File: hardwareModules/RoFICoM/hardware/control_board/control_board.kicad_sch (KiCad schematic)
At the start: 35 parts, among them J1 BoardSkirtConnector, J2 M+, J3 M-, J4 SYS_CONN, J5 PWR_CONN_1, J6 PWR_CONN_2, J7 CableConnector, J8 CablePads, J9 SkirtPads, U1 STM32G071GBU6, U2 DRV8837C, U3 HX6306P332MR, U4 KTH1611SH-SF5, U5 KTH1611SH-SF5

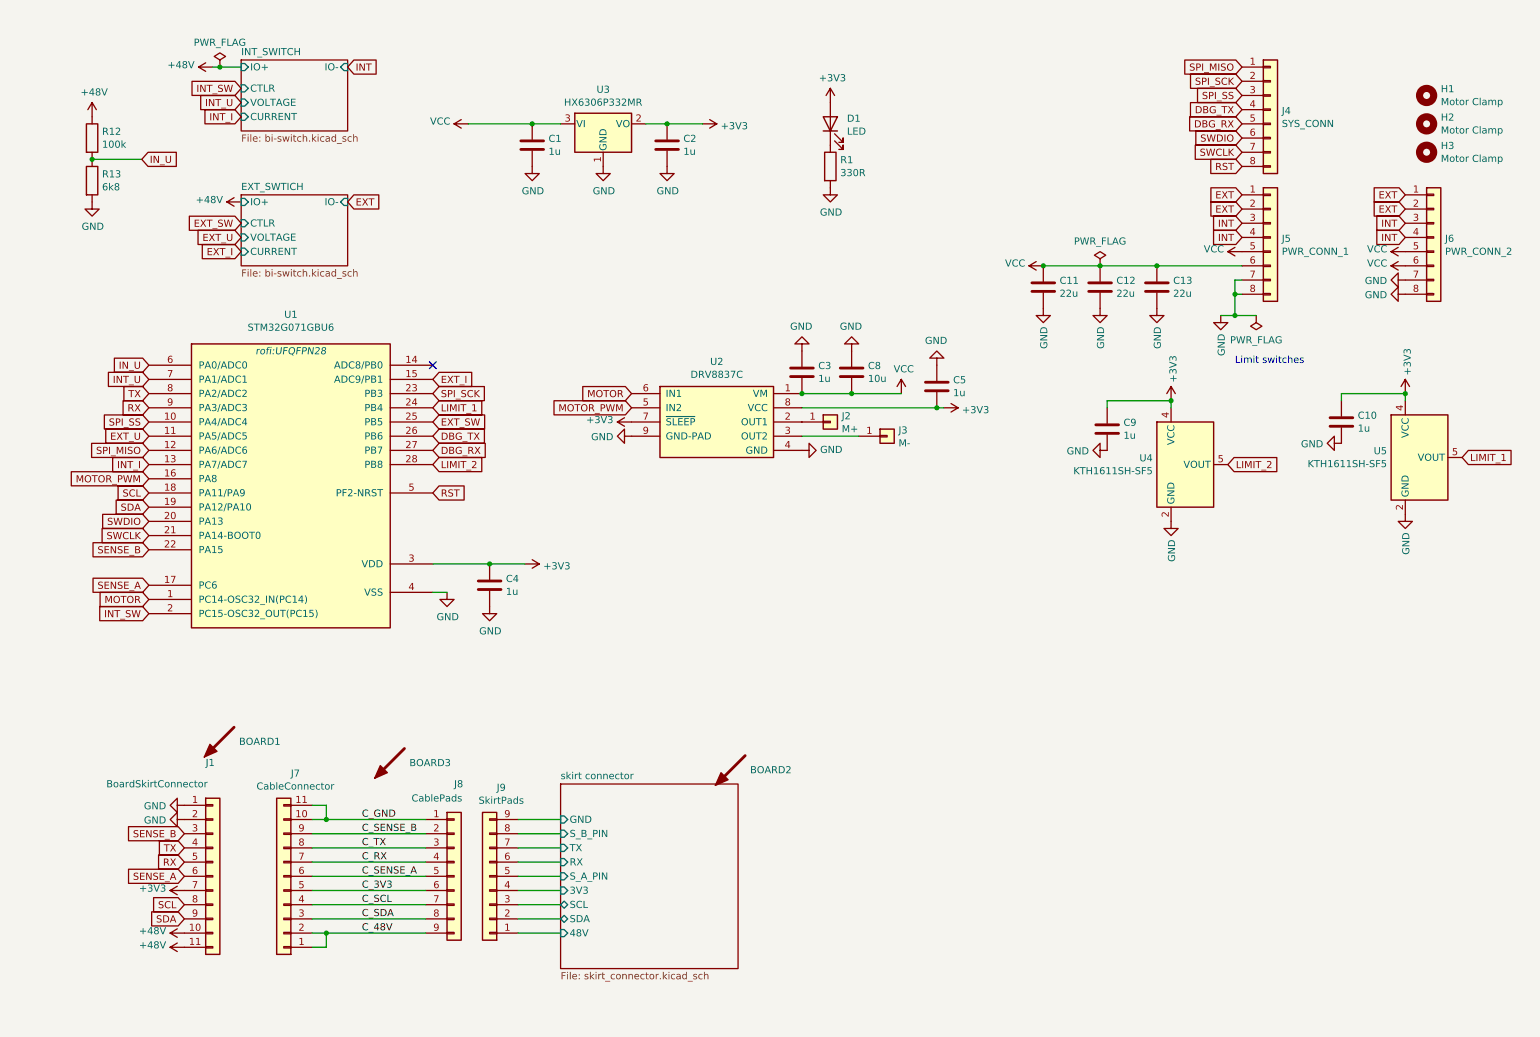
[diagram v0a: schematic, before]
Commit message: roficom: Implement v1 hardware
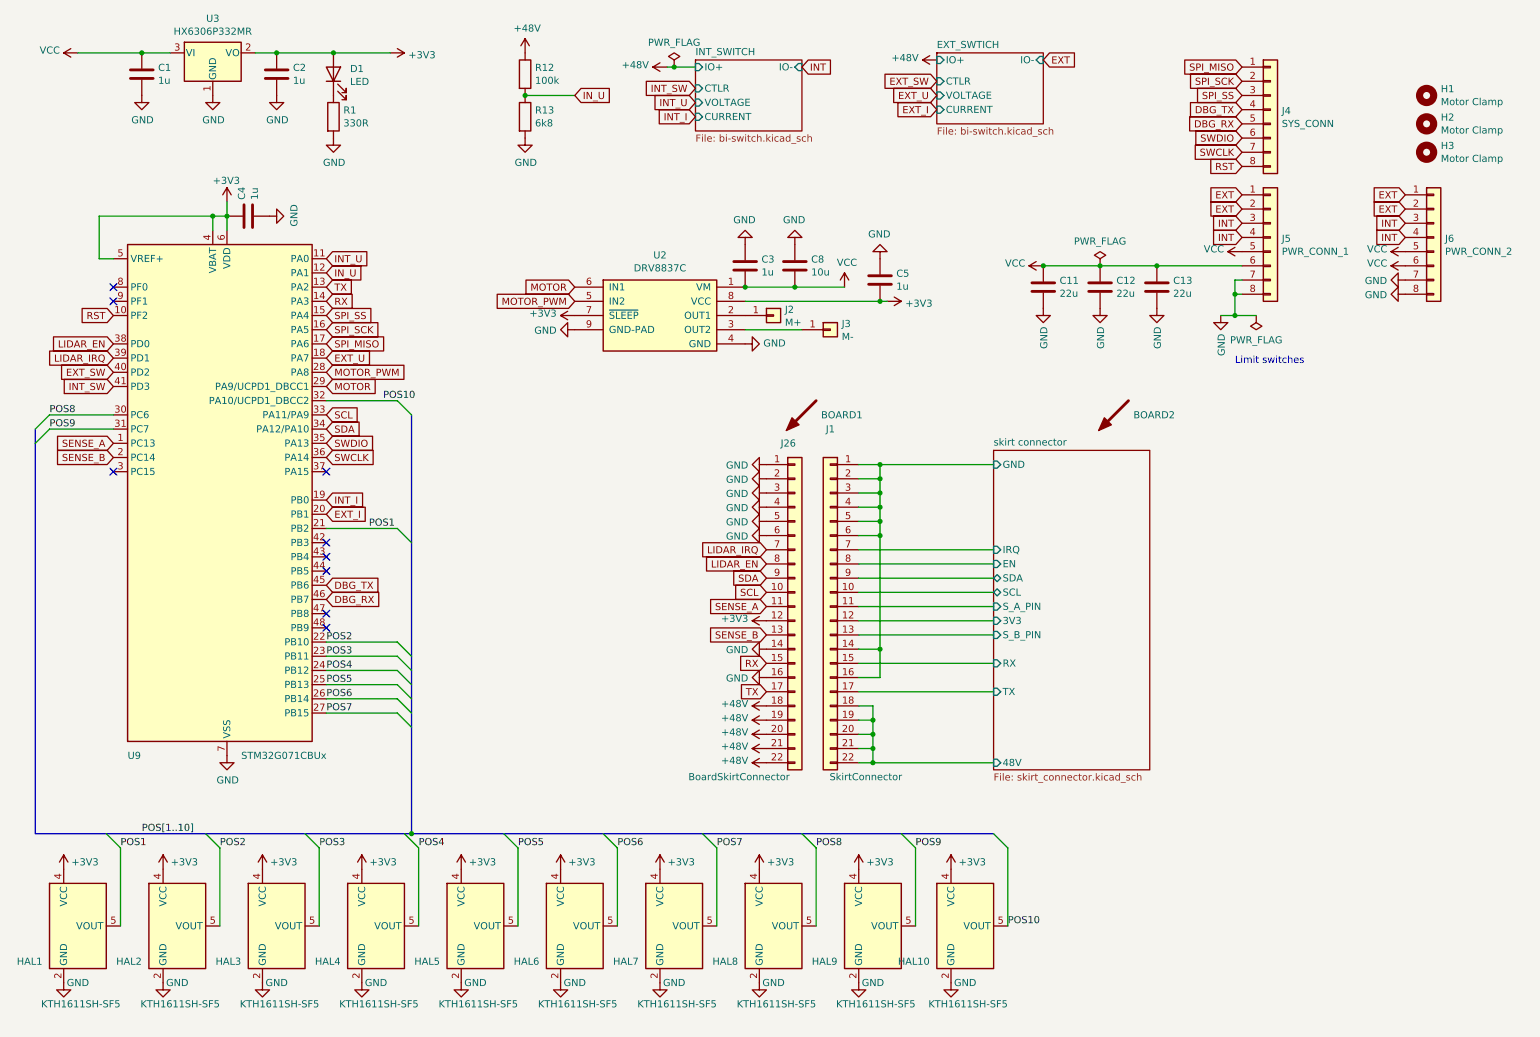
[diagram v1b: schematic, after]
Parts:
- removed BOARD3: BOARD, kikit:Board, symbol Graphic:SYM_Arrow45_Large
- removed C10, C9: 1u, Capacitor_SMD:C_0402_1005Metric, symbol Device:C
- removed J1: BoardSkirtConnector, rofi:FC38-11N1-AHK, symbol Connector_Generic:Conn_01x11
- removed J7: CableConnector, rofi:FPC_PADS_11, symbol Connector_Generic:Conn_01x11
- removed J8: CablePads, rofi:RoFICoM_CableFPCPads, symbol Connector_Generic:Conn_01x09
- removed J9: SkirtPads, rofi:RoFICoM_CablePads, symbol Connector_Generic:Conn_01x09
- removed U1: STM32G071GBU6, rofi:UFQFPN28, symbol rofi:STM32G071GBU6
- removed U4, U5: KTH1611SH-SF5, Package_TO_SOT_SMD:SOT-553, symbol rofi:KTH1611SH-SF5
- added HAL1, HAL10, HAL2, HAL3, HAL4, HAL5, HAL6, HAL7, HAL8, HAL9: KTH1611SH-SF5, Package_TO_SOT_SMD:SOT-553, symbol rofi:KTH1611SH-SF5
- added J1: SkirtConnector, rofi:FPC_0.5_22_PADS, symbol Connector_Generic:Conn_01x22
- added J26: BoardSkirtConnector, rofi:781272210, symbol Connector_Generic:Conn_01x22
- added U9: STM32G071CBUx, Package_DFN_QFN:QFN-48-1EP_7x7mm_P0.5mm_EP5.6x5.6mm, symbol STM32G0:STM32G071CBUx
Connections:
- net +3V3: now also HAL1.4 (VCC), HAL10.4 (VCC), HAL2.4 (VCC), HAL3.4 (VCC), HAL4.4 (VCC), HAL5.4 (VCC), HAL6.4 (VCC), HAL7.4 (VCC), HAL8.4 (VCC), HAL9.4 (VCC), J26.12 (Pin_12), U9.4 (VBAT), U9.5 (VREF+), U9.6 (VDD)
- net +48V: now also J26.18 (Pin_18), J26.19 (Pin_19), J26.20 (Pin_20), J26.21 (Pin_21), J26.22 (Pin_22)
- net DBG_RX: now also U9.46 (PB7)
- net DBG_TX: now also U9.45 (PB6)
- net EXT_I: now also U9.20 (PB1)
- net EXT_SW: now also U9.40 (PD2)
- net EXT_U: now also U9.18 (PA7)
- net GND: now also HAL1.2 (GND), HAL10.2 (GND), HAL2.2 (GND), HAL3.2 (GND), HAL4.2 (GND), HAL5.2 (GND), HAL6.2 (GND), HAL7.2 (GND), HAL8.2 (GND), HAL9.2 (GND), J26.1 (Pin_1), J26.14 (Pin_14), J26.16 (Pin_16), J26.2 (Pin_2), J26.3 (Pin_3), J26.4 (Pin_4), J26.5 (Pin_5), J26.6 (Pin_6), U9.49 (VSS), U9.7 (VSS)
- net INT_I: now also U9.19 (PB0)
- net INT_SW: now also U9.41 (PD3)
- net INT_U: now also U9.11 (PA0)
- net IN_U: now also U9.12 (PA1)
- net MOTOR: now also U9.29 (PA9/UCPD1_DBCC1)
- net MOTOR_PWM: now also U9.28 (PA8)
- net RST: now also U9.10 (PF2)
- net RX: now also J26.15 (Pin_15), U9.14 (PA3)
- net SCL: now also J26.10 (Pin_10), U9.33 (PA11/PA9)
- net SDA: now also J26.9 (Pin_9), U9.34 (PA12/PA10)
- net SENSE_A: now also J26.11 (Pin_11), U9.1 (PC13)
- net SENSE_B: now also J26.13 (Pin_13), U9.2 (PC14)
- net SPI_MISO: now also U9.17 (PA6)
- net SPI_SCK: now also U9.16 (PA5)
- net SPI_SS: now also U9.15 (PA4)
- net SWCLK: now also U9.36 (PA14)
- net SWDIO: now also U9.35 (PA13)
- net TX: now also J26.17 (Pin_17), U9.13 (PA2)
- net skirt connector/3V3: now also J1.12 (Pin_12)
- net skirt connector/48V: now also J1.18 (Pin_18), J1.19 (Pin_19), J1.20 (Pin_20), J1.21 (Pin_21), J1.22 (Pin_22)
- net skirt connector/GND: now also J1.1 (Pin_1), J1.14 (Pin_14), J1.16 (Pin_16), J1.2 (Pin_2), J1.3 (Pin_3), J1.4 (Pin_4), J1.5 (Pin_5), J1.6 (Pin_6)
- net skirt connector/RX: now also J1.15 (Pin_15)
- net skirt connector/SCL: now also J1.10 (Pin_10)
- net skirt connector/SDA: now also J1.9 (Pin_9)
- net skirt connector/S_A_PIN: now also J1.11 (Pin_11)
- net skirt connector/S_B_PIN: now also J1.13 (Pin_13)
- net skirt connector/TX: now also J1.17 (Pin_17)
- new net LIDAR_EN: J26.8 (Pin_8), U9.38 (PD0)
- new net LIDAR_IRQ: J26.7 (Pin_7), U9.39 (PD1)
- new net POS1: HAL1.5 (VOUT), U9.21 (PB2)
- new net POS10: HAL10.5 (VOUT), U9.32 (PA10/UCPD1_DBCC2)
- new net POS2: HAL2.5 (VOUT), U9.22 (PB10)
- new net POS3: HAL3.5 (VOUT), U9.23 (PB11)
- new net POS4: HAL4.5 (VOUT), U9.24 (PB12)
- new net POS5: HAL5.5 (VOUT), U9.25 (PB13)
- new net POS6: HAL6.5 (VOUT), U9.26 (PB14)
- new net POS7: HAL7.5 (VOUT), U9.27 (PB15)
- new net POS8: HAL8.5 (VOUT), U9.30 (PC6)
- new net POS9: HAL9.5 (VOUT), U9.31 (PC7)
- new net skirt connector/EN: J1.8 (Pin_8)
- new net skirt connector/IRQ: J1.7 (Pin_7)
- no-connect marks 1 -> 9
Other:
- sheet skirt connector ports: added EN, IRQ; removed none
- moved on the sheet: BOARD1, BOARD2, C1, C2, C3, C4, C5, C8, D1, J2, J3, R1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

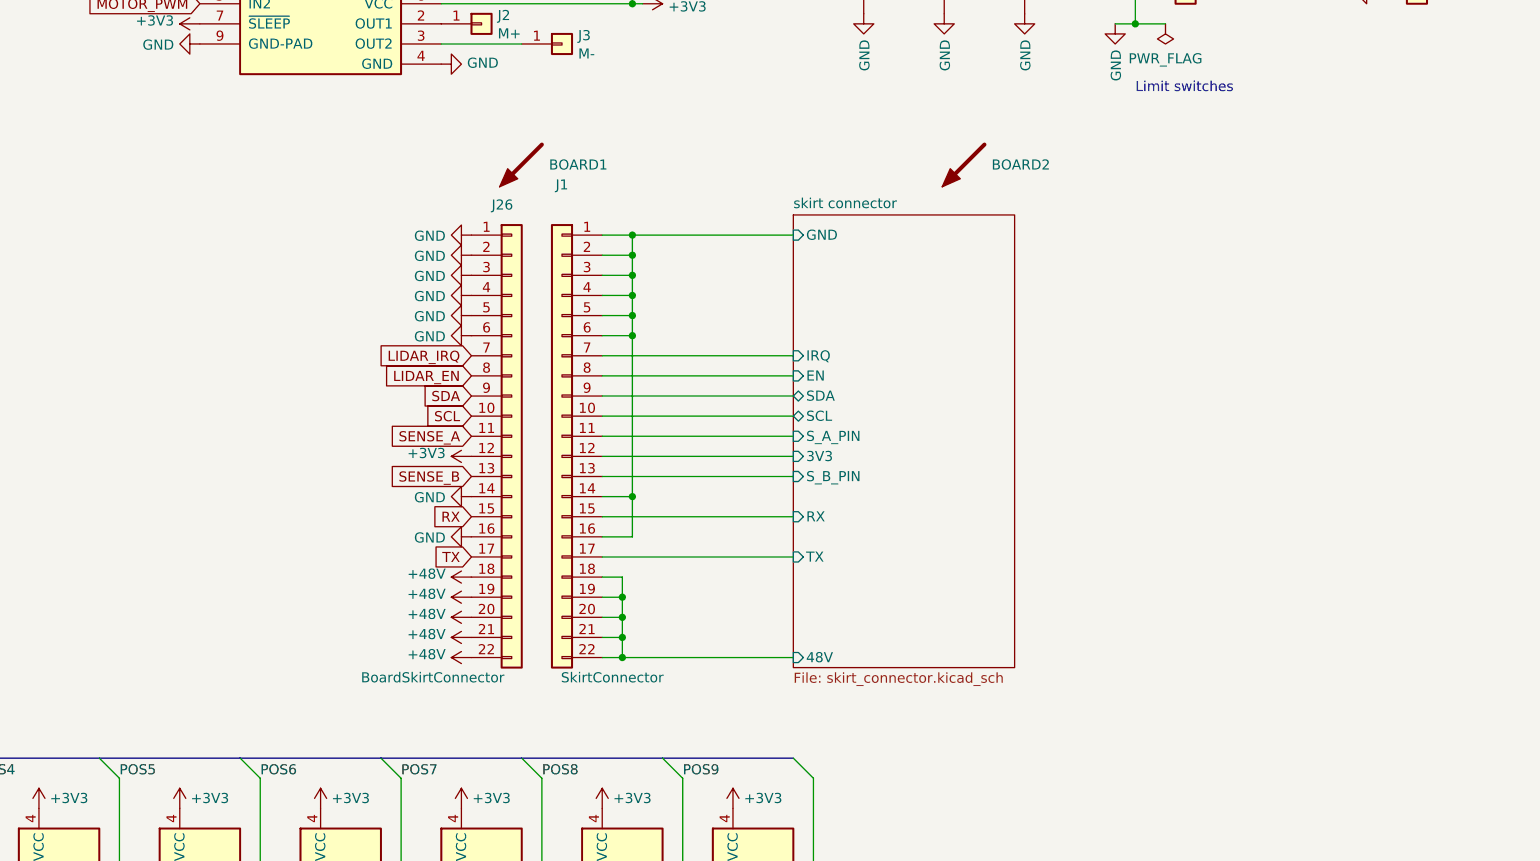
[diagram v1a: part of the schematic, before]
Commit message: hardware: Add custom FPC cables
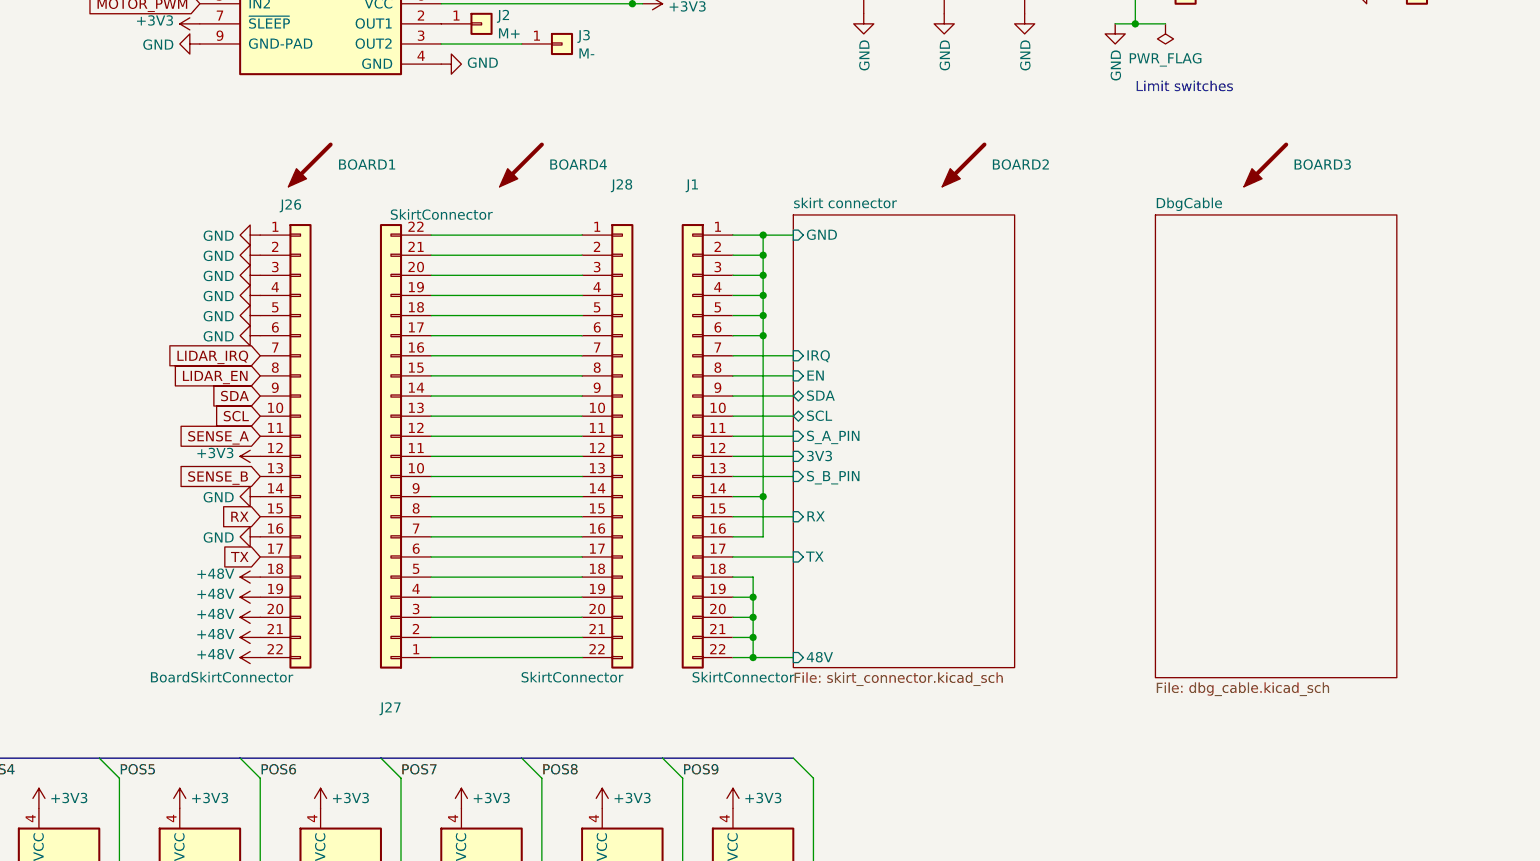
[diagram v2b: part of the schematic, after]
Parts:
- added BOARD3, BOARD4: BOARD, kikit:Board, symbol Graphic:SYM_Arrow45_Large
- added J27, J28: SkirtConnector, rofi:FPC_0.5_22_PADS, symbol Connector_Generic:Conn_01x22
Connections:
- new net: J27.1 (Pin_1), J28.22 (Pin_22)
- new net: J27.10 (Pin_10), J28.13 (Pin_13)
- new net: J27.11 (Pin_11), J28.12 (Pin_12)
- new net: J27.12 (Pin_12), J28.11 (Pin_11)
- new net: J27.13 (Pin_13), J28.10 (Pin_10)
- new net: J27.14 (Pin_14), J28.9 (Pin_9)
- new net: J27.15 (Pin_15), J28.8 (Pin_8)
- new net: J27.16 (Pin_16), J28.7 (Pin_7)
- new net: J27.17 (Pin_17), J28.6 (Pin_6)
- new net: J27.18 (Pin_18), J28.5 (Pin_5)
- new net: J27.19 (Pin_19), J28.4 (Pin_4)
- new net: J27.2 (Pin_2), J28.21 (Pin_21)
- new net: J27.20 (Pin_20), J28.3 (Pin_3)
- new net: J27.21 (Pin_21), J28.2 (Pin_2)
- new net: J27.22 (Pin_22), J28.1 (Pin_1)
- new net: J27.3 (Pin_3), J28.20 (Pin_20)
- new net: J27.4 (Pin_4), J28.19 (Pin_19)
- new net: J27.5 (Pin_5), J28.18 (Pin_18)
- new net: J27.6 (Pin_6), J28.17 (Pin_17)
- new net: J27.7 (Pin_7), J28.16 (Pin_16)
- new net: J27.8 (Pin_8), J28.15 (Pin_15)
- new net: J27.9 (Pin_9), J28.14 (Pin_14)
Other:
- added sheet DbgCable (dbg_cable.kicad_sch)
- moved on the sheet: BOARD1, J1, J26
